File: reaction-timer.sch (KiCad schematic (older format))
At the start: 0 parts

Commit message: Add the control section of the schematic
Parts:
- added C1, C5: CP, symbol CP
- added C2, C3, C4, C6: C, symbol C
- added IC5, IC6, IC7: NE555P, symbol NE555P
- added LED1: LED, symbol LED
- added R10, R11, R12, R13, R7, R9: R, symbol R
- added R8: POT, symbol POT
- added S3, S4: SW_PUSH, symbol SW_PUSH
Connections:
- net labels added: +9V, GNDREF
- wire segments 0 -> 59
- no-connect marks 0 -> 3
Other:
- note added: "Clock"
- note added: "Delay"
- note added: "Start Delay"
- note added: "Stop"

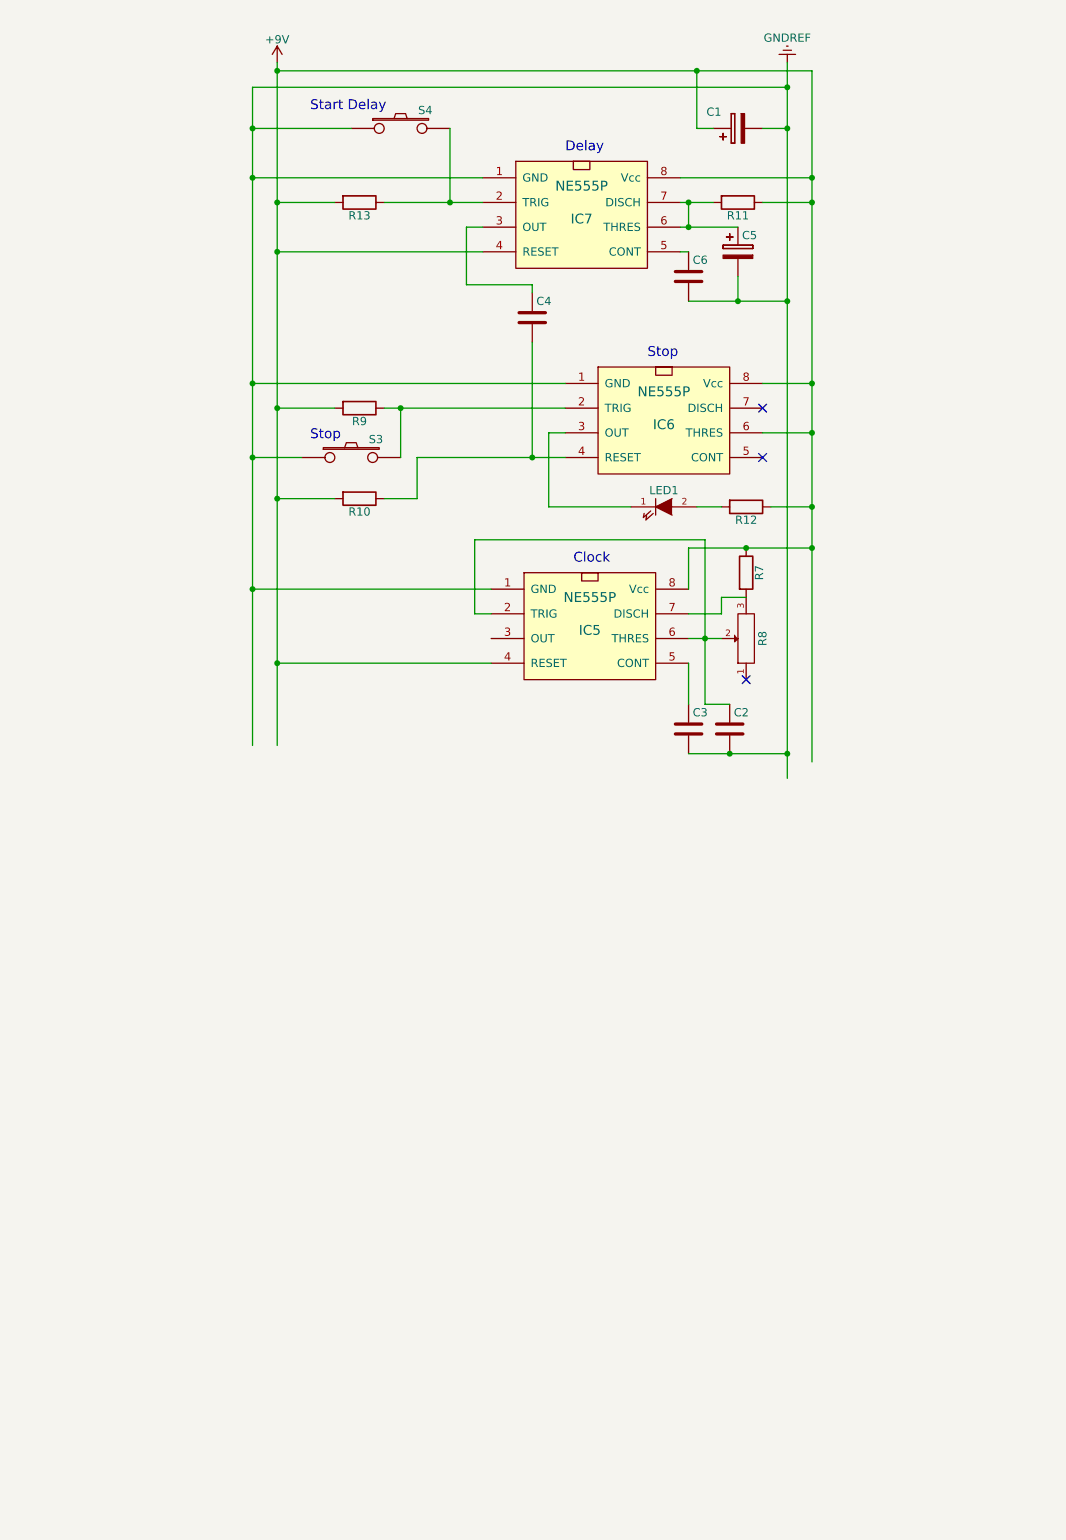
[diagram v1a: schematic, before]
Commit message: Add 4026 decade counters to schematic
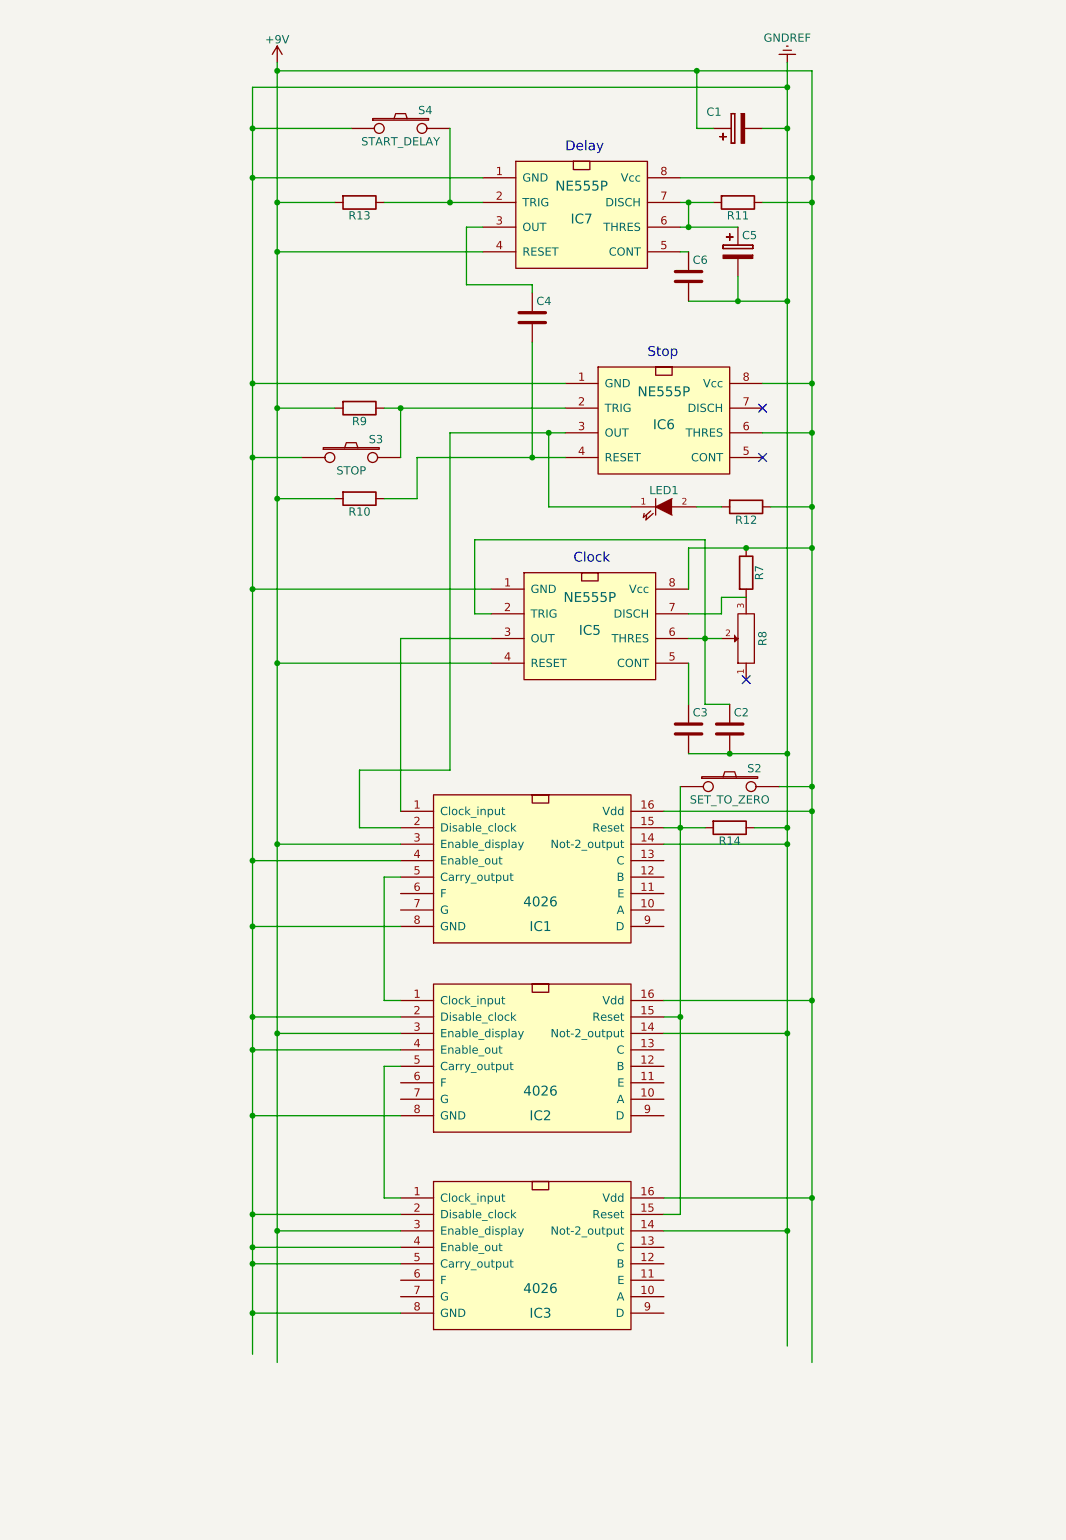
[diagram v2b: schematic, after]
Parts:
- added IC1, IC2, IC3: 4026, symbol 4026
- added R14: R, symbol R
- added S2: SET_TO_ZERO, symbol SW_PUSH
- S3: value SW_PUSH -> STOP
- S4: value SW_PUSH -> START_DELAY
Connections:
- wire segments 59 -> 95
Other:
- note removed: "Start Delay"
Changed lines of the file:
@@
 P 3400 1300
 F 0 "S4" H 3550 1410 50  0000 C CNN
-F 1 "SW_PUSH" H 3400 1220 50  0001 C CNN
+F 1 "START_DELAY" H 3400 1220 50  0000 C CNN
 F 2 "" H 3400 1300 60  0000 C CNN
 F 3 "" H 3400 1300 60  0000 C CNN
@@
 $EndComp
 $Comp
-L +9V #PWR?
+L +9V #PWR01
 U 1 1 557464E7
 P 2650 900
-F 0 "#PWR?" H 2650 750 50  0001 C CNN
+F 0 "#PWR01" H 2650 750 50  0001 C CNN
 F 1 "+9V" H 2650 1040 50  0000 C CNN
 F 2 "" H 2650 900 60  0000 C CNN
@@
 $EndComp
 $Comp
-L GNDREF #PWR?
+L GNDREF #PWR02
 U 1 1 557465F3
 P 5750 900
-F 0 "#PWR?" H 5750 650 50  0001 C CNN
+F 0 "#PWR02" H 5750 650 50  0001 C CNN
 F 1 "GNDREF" H 5750 750 50  0000 C CNN
 F 2 "" H 5750 900 60  0000 C CNN
@@
 P 3100 3300
 F 0 "S3" H 3250 3410 50  0000 C CNN
-F 1 "SW_PUSH" H 3100 3220 50  0001 C CNN
+F 1 "STOP" H 3100 3220 50  0000 C CNN
 F 2 "" H 3100 3300 60  0000 C CNN
 F 3 "" H 3100 3300 60  0000 C CNN
@@
 	1    0    0    -1
 $EndComp
-Text Notes 2850 1200 0    60   ~ 0
-Start Delay
-Text Notes 2850 3200 0    60   ~ 0
-Stop
 $Comp
 L POT R8
@@
 NoConn ~ 5500 4650
 Wire Wire Line
-	5750 900  5750 5250
+	5750 900  5750 8700
 Wire Wire Line
 	5750 1050 2500 1050
 Wire Wire Line
-	2500 1050 2500 5050
+	2500 1050 2500 8750
 Wire Wire Line
 	3100 1300 2500 1300
@@
 	3700 1750 3700 1300
 Wire Wire Line
-	2650 900  2650 5050
+	2650 900  2650 8800
 Wire Wire Line
 	3900 1600 2500 1600
@@
 	2650 950  5900 950
 Wire Wire Line
-	5900 950  5900 5150
+	5900 950  5900 8800
 Wire Wire Line
 	5300 1300 5200 1300
@@
 	4300 3600 4300 3150
 Wire Wire Line
-	4300 3150 4400 3150
+	3700 3150 4400 3150
 Wire Wire Line
 	5350 3600 5200 3600
@@
 Wire Wire Line
 	5250 4800 5400 4800
+$Comp
+L 4026 IC1
+U 1 1 55747860
+P 4250 6050
+F 0 "IC1" H 4250 5950 60  0000 C CNN
+F 1 "4026" H 4250 6100 60  0000 C CNN
+F 2 "" H 4250 6050 60  0000 C CNN
+F 3 "" H 4250 6050 60  0000 C CNN
+	1    4250 6050
+	1    0    0    -1
+$EndComp
+Wire Wire Line
+	5000 5450 5900 5450
+Connection ~ 5900 5450
+$Comp
+L SW_PUSH S2
+U 1 1 55747C3F
+P 5400 5300
+F 0 "S2" H 5550 5410 50  0000 C CNN
+F 1 "SET_TO_ZERO" H 5400 5220 50  0000 C CNN
+F 2 "" H 5400 5300 60  0000 C CNN
+F 3 "" H 5400 5300 60  0000 C CNN
+	1    5400 5300
+	1    0    0    -1
+$EndComp
+Wire Wire Line
+	5700 5300 5900 5300
+Connection ~ 5900 5300
+Wire Wire Line
+	5100 5300 5100 7900
+Wire Wire Line
+	5000 5550 5250 5550
+$Comp
+L R R14
+U 1 1 55748AEB
+P 5400 5550
+F 0 "R14" V 5480 5550 50  0000 C CNN
+F 1 "R" V 5400 5550 50  0001 C CNN
+F 2 "" V 5330 5550 30  0000 C CNN
+F 3 "" H 5400 5550 30  0000 C CNN
+	1    5400 5550
+	0    1    1    0
+$EndComp
+Connection ~ 5100 5550
+Wire Wire Line
+	5550 5550 5750 5550
+Connection ~ 5750 5550
+Wire Wire Line
+	3950 4400 3400 4400
+Wire Wire Line
+	3400 4400 3400 5450
+Wire Wire Line
+	3700 3150 3700 5200
+Wire Wire Line
+	3700 5200 3150 5200
+Wire Wire Line
+	3150 5200 3150 5550
+Wire Wire Line
+	3150 5550 3400 5550
+Connection ~ 4300 3150
+$Comp
+L 4026 IC2
+U 1 1 55749C9B
+P 4250 7200
+F 0 "IC2" H 4250 7100 60  0000 C CNN
+F 1 "4026" H 4250 7250 60  0000 C CNN
+F 2 "" H 4250 7200 60  0000 C CNN
+F 3 "" H 4250 7200 60  0000 C CNN
+	1    4250 7200
+	1    0    0    -1
+$EndComp
+$Comp
+L 4026 IC3
+U 1 1 5574A0BA
+P 4250 8400
+F 0 "IC3" H 4250 8300 60  0000 C CNN
+F 1 "4026" H 4250 8450 60  0000 C CNN
+F 2 "" H 4250 8400 60  0000 C CNN
+F 3 "" H 4250 8400 60  0000 C CNN
+	1    4250 8400
+	1    0    0    -1
+$EndComp
+Wire Wire Line
+	3400 5850 3300 5850
+Wire Wire Line
+	3300 5850 3300 6600
+Wire Wire Line
+	3300 6600 3400 6600
+Wire Wire Line
+	3400 7000 3300 7000
+Wire Wire Line
+	3300 7000 3300 7800
+Wire Wire Line
+	3300 7800 3400 7800
+Wire Wire Line
+	3400 5650 2650 5650
+Connection ~ 2650 5650
+Wire Wire Line
+	3400 5750 2500 5750
+Connection ~ 2500 5750
+Wire Wire Line
+	3400 6150 2500 6150
+Connection ~ 2500 6150
+Wire Wire Line
+	3400 6700 2500 6700
+Connection ~ 2500 6700
+Wire Wire Line
+	3400 6800 2650 6800
+Connection ~ 2650 6800
+Wire Wire Line
+	3400 6900 2500 6900
+Connection ~ 2500 6900
+Wire Wire Line
+	3400 7300 2500 7300
+Connection ~ 2500 7300
+Wire Wire Line
+	3400 7900 2500 7900
+Connection ~ 2500 7900
+Wire Wire Line
+	3400 8000 2650 8000
+Connection ~ 2650 8000
+Wire Wire Line
+	3400 8100 2500 8100
+Connection ~ 2500 8100
+Wire Wire Line
+	3400 8200 2500 8200
+Connection ~ 2500 8200
+Wire Wire Line
+	3400 8500 2500 8500
+Connection ~ 2500 8500
+Wire Wire Line
+	5000 5650 5750 5650
+Connection ~ 5750 5650
+Wire Wire Line
+	5000 6600 5900 6600
+Connection ~ 5900 6600
+Wire Wire Line
+	5100 6700 5000 6700
+Wire Wire Line
+	5100 7900 5000 7900
+Connection ~ 5100 6700
+Wire Wire Line
+	5000 6800 5750 6800
+Connection ~ 5750 6800
+Wire Wire Line
+	5000 7800 5900 7800
+Connection ~ 5900 7800
+Wire Wire Line
+	5000 8000 5750 8000
+Connection ~ 5750 8000
 $EndSCHEMATC

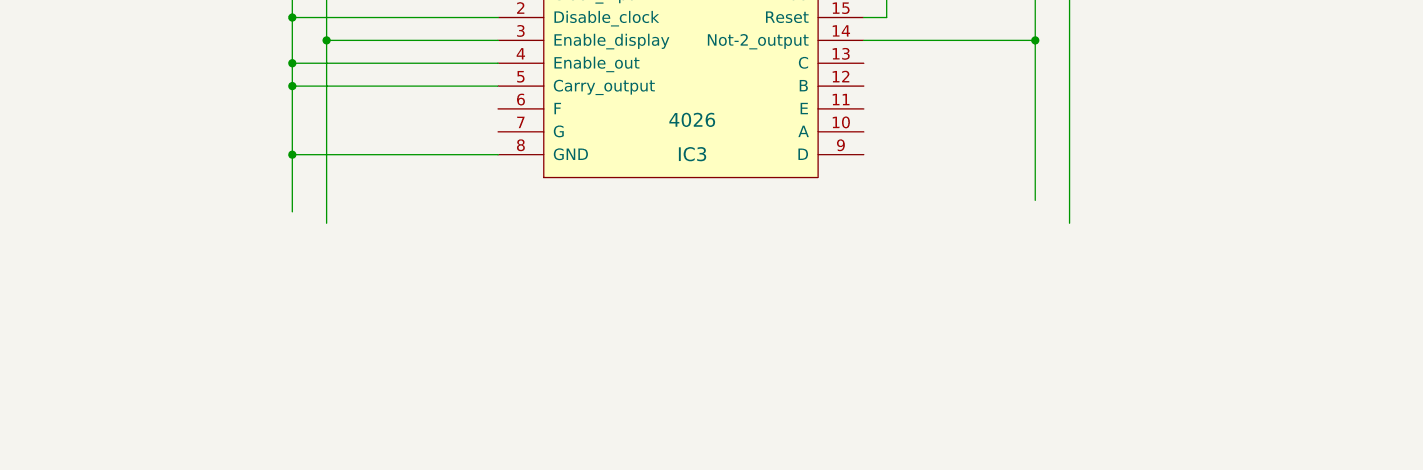
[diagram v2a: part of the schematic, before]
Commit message: Add 7-segment displays
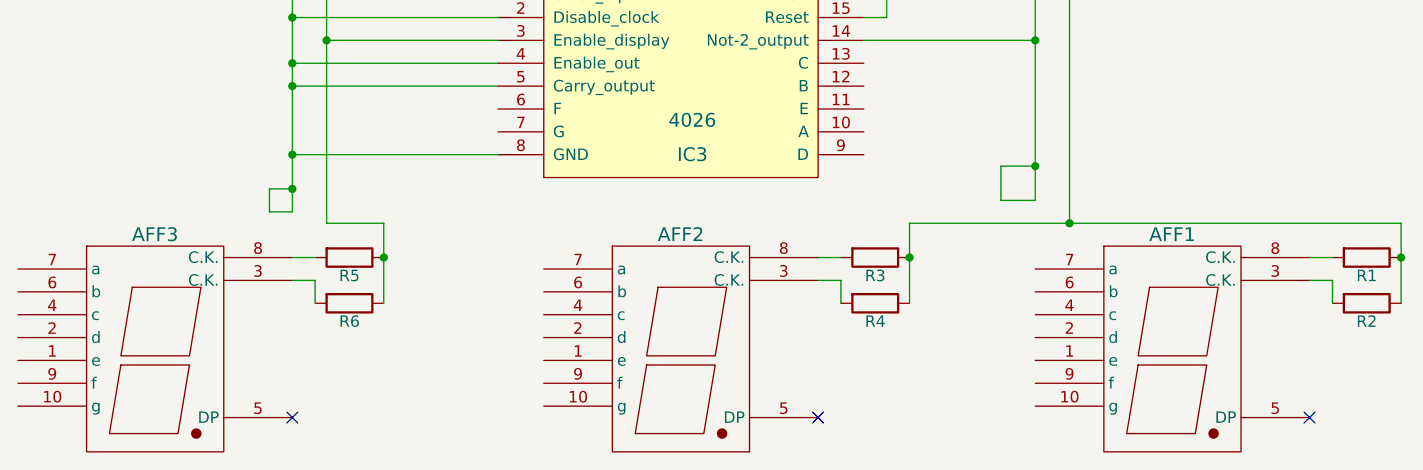
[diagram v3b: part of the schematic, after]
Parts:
- added AFF1, AFF2, AFF3: LTS-6980HR, symbol LTS-6980HR
- added R1, R2, R3, R4, R5, R6: R, symbol R
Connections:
- wire segments 95 -> 115
- no-connect marks 3 -> 6

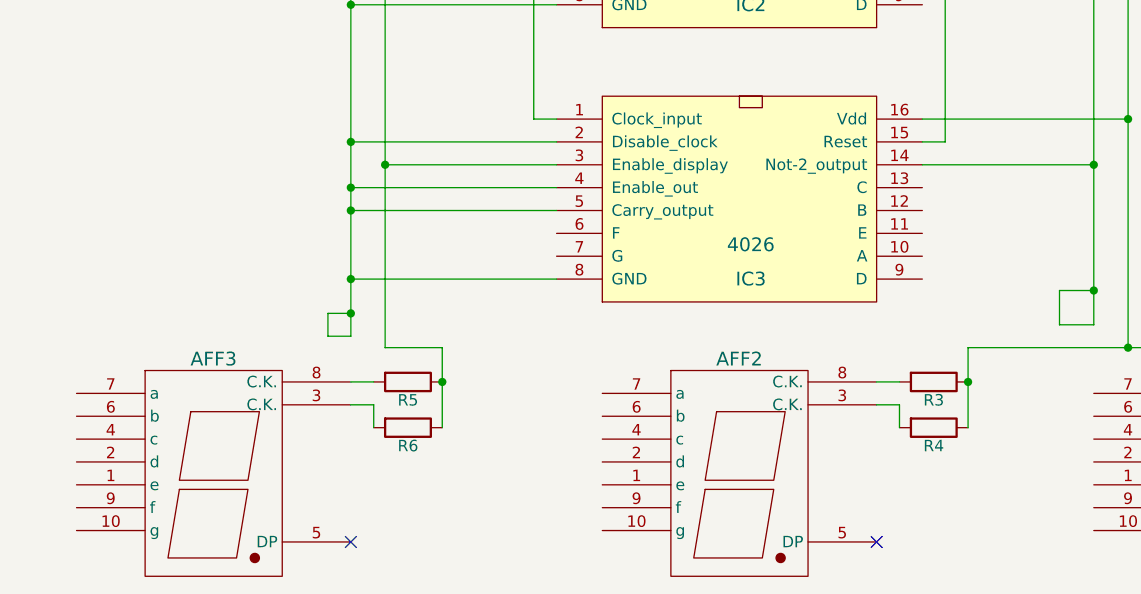
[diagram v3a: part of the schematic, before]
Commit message: Add connections to most significant digit display
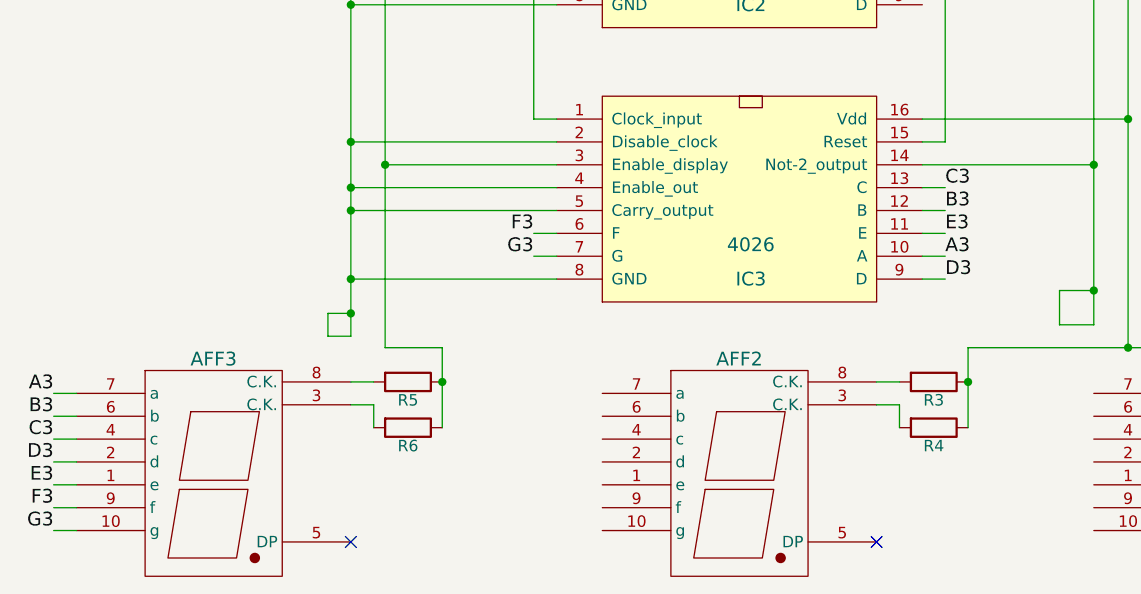
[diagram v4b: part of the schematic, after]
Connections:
- net A3: now reaches IC3.10 (A)
- net A3: now also AFF3.7 (a)
- net E3: now reaches IC3.11 (E)
- net E3: now also AFF3.1 (e)
- net B3: now reaches IC3.12 (B)
- net B3: now also AFF3.6 (b)
- net C3: now reaches IC3.13 (C)
- net C3: now also AFF3.4 (c)
- net F3: now reaches IC3.6 (F)
- net F3: now also AFF3.9 (f)
- net G3: now reaches IC3.7 (G)
- net G3: now also AFF3.10 (g)
- net D3: now reaches IC3.9 (D)
- net D3: now also AFF3.2 (d)
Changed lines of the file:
@@
 Connection ~ 5900 8800
 Connection ~ 5200 8950
+Text Label 1200 9000 2    60   ~ 0
+A3
+Text Label 5100 8400 0    60   ~ 0
+A3
+Wire Wire Line
+	5000 8400 5100 8400
+Wire Wire Line
+	1200 9000 1300 9000
+Text Label 1200 9100 2    60   ~ 0
+B3
+Text Label 1200 9200 2    60   ~ 0
+C3
+Text Label 1200 9300 2    60   ~ 0
+D3
+Text Label 1200 9400 2    60   ~ 0
+E3
+Text Label 1200 9500 2    60   ~ 0
+F3
+Text Label 1200 9600 2    60   ~ 0
+G3
+Text Label 3300 8400 2    60   ~ 0
+G3
+Text Label 3300 8300 2    60   ~ 0
+F3
+Wire Wire Line
+	3300 8300 3400 8300
+Wire Wire Line
+	3300 8400 3400 8400
+Wire Wire Line
+	1200 9100 1300 9100
+Wire Wire Line
+	1200 9200 1300 9200
+Wire Wire Line
+	1200 9300 1300 9300
+Wire Wire Line
+	1200 9400 1300 9400
+Wire Wire Line
+	1200 9500 1300 9500
+Wire Wire Line
+	1200 9600 1300 9600
+Text Label 5100 8500 0    60   ~ 0
+D3
+Text Label 5100 8100 0    60   ~ 0
+C3
+Text Label 5100 8200 0    60   ~ 0
+B3
+Text Label 5100 8300 0    60   ~ 0
+E3
+Wire Wire Line
+	5000 8500 5100 8500
+Wire Wire Line
+	5000 8300 5100 8300
+Wire Wire Line
+	5000 8200 5100 8200
+Wire Wire Line
+	5000 8100 5100 8100
 $EndSCHEMATC
